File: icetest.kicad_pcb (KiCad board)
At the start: 2 copper layers, 66.7 x 57.2 mm, 50 parts

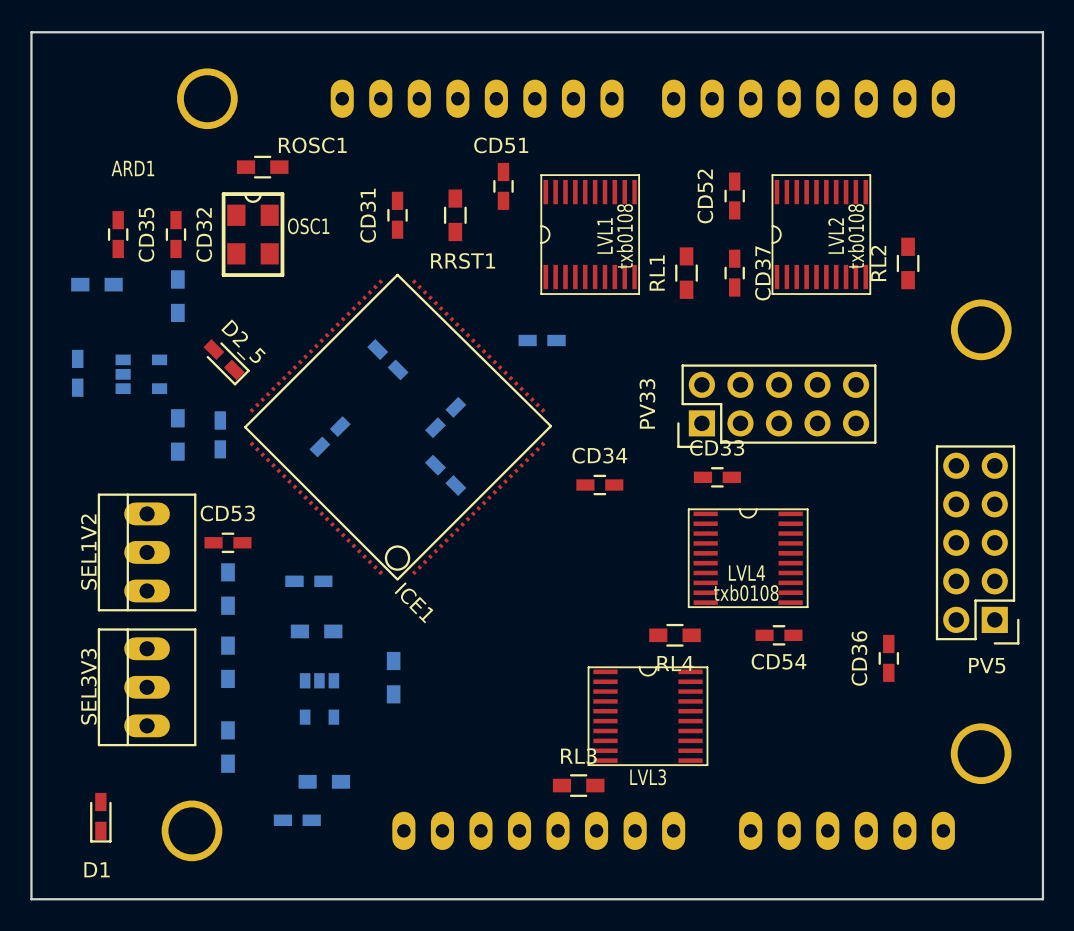
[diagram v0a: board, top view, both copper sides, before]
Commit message: add SPI test points and verify footprints
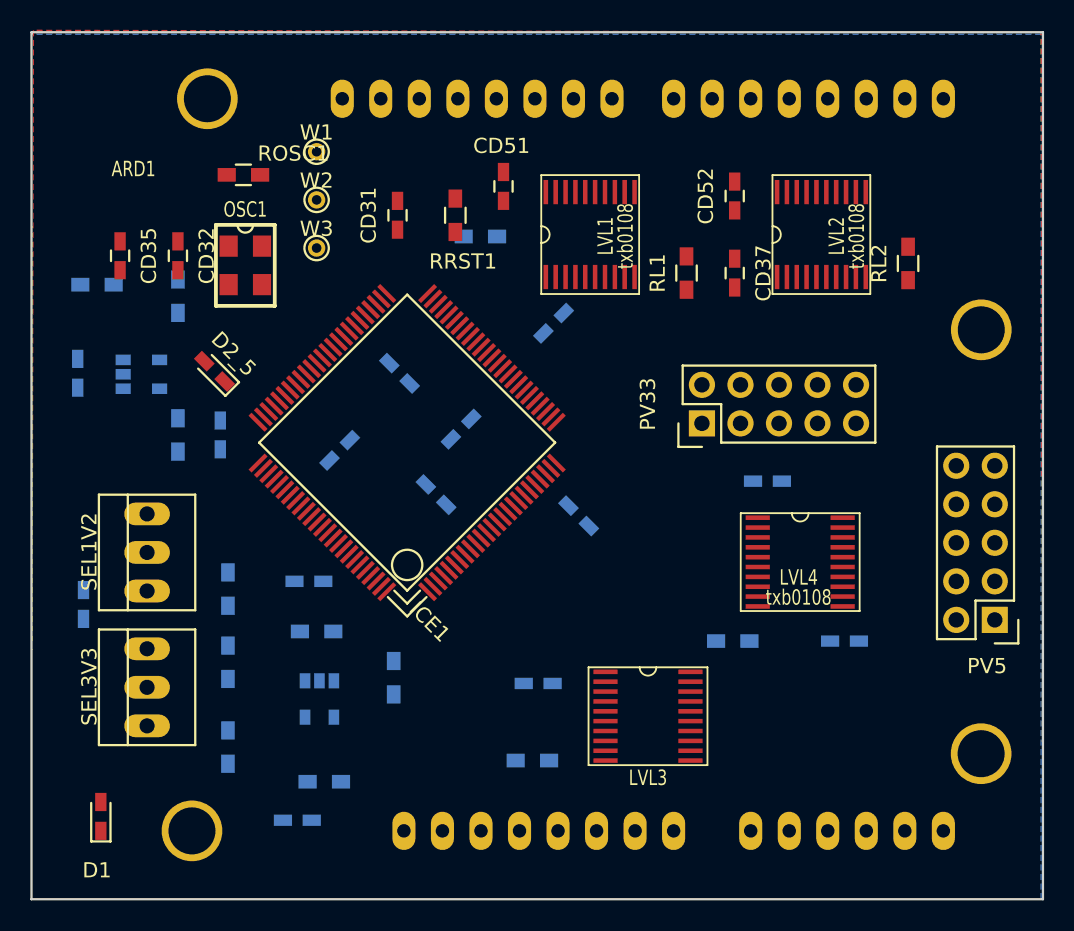
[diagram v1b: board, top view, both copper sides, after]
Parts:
- added RSS1: 10k, Resistors_SMD:R_0603_HandSoldering, B.Cu at (152.8, 106.8)
- added W1: TEST_1P, Connect:PINTST, F.Cu at (142.0, 101.2)
- added W2: TEST_1P, Connect:PINTST, F.Cu at (142.0, 104.4)
- added W3: TEST_1P, Connect:PINTST, F.Cu at (142.0, 107.6)
- CD33, CD34, CD36, CD53, CD54, RL3, RL4: moved to B.Cu
- moved CD36 23.2 mm to (156.6, 136.3), turned to 180 degrees
- moved CD53 10.4 mm to (126.6, 131.1), turned to 270 degrees
- moved CD54 4.33 mm to (176.8, 133.5)
- moved RL4 3.83 mm to (169.4, 133.5)
- moved RL3 3.47 mm to (156.2, 141.4), turned to 180 degrees
- moved LVL4 3.44 mm to (173.9, 128.3)
- moved CD33 3.31 mm to (171.7, 122.9), turned to 180 degrees
- moved CD34 2.47 mm to (159.3, 125.2), turned to 315 degrees
- moved OSC1 2.09 mm to (137.3, 108.7)
- moved CD13 1.42 mm to (149.9, 123.8)
- moved CD32 1.40 mm to (132.8, 108.1)
- moved CD35 1.40 mm to (129.0, 108.1)
- moved CD38 1.37 mm to (157.6, 112.5), turned to 45 degrees
- moved ROSC1 1.37 mm to (137.2, 102.7)
- moved CD14 1.27 mm to (151.5, 119.5)
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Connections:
- CR32 pad 1: GND -> /r3V3
- CR32 pad 2: /r3V3 -> GND
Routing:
- added copper zone on B.Cu, net GND
- added copper zone on F.Cu, net GND
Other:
- net class Ground added: clearance 0.152, trace_width 0.2, via_dia 0.6, via_drill 0.4

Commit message: route it
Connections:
- ARD1 pad 33: (no net) -> GND
- ARD1 pad 34: (no net) -> GND
- ARD1 pad 35: (no net) -> GND
- ARD1 pad 36: (no net) -> GND
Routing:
- net +3V3: track 0.00 -> 213.1 mm, vias 0 -> 4
- net +5V: track 0.00 -> 180.2 mm
- net GND: track 0.00 -> 91.6 mm, vias 0 -> 25
- net VCC: track 0.00 -> 63.9 mm, vias 0 -> 3
- net /FPGA/D5+: track 0.00 -> 52.1 mm, vias 0 -> 1
- net /r3V3: track 0.00 -> 37.1 mm, vias 0 -> 1
- net Net-(ICE1-Pad100): track 0.00 -> 32.7 mm, vias 0 -> 2
- net /FPGA/D5-: track 0.00 -> 32.5 mm, vias 0 -> 1
- net /Arduino Shield/SCK: track 0.00 -> 29.6 mm
- net /Arduino Shield/a3V3: track 0.00 -> 28.9 mm
- net /Arduino Shield/LOG_L3E: track 0.00 -> 28.6 mm, vias 0 -> 2
- net /Arduino Shield/LOG_L2E: track 0.00 -> 27.8 mm
- net /Arduino Shield/ANA0: track 0.00 -> 26.5 mm
- net /Arduino Shield/ANA1: track 0.00 -> 25.4 mm
- net /Arduino Shield/DIG4: track 0.00 -> 25.3 mm, vias 0 -> 2
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
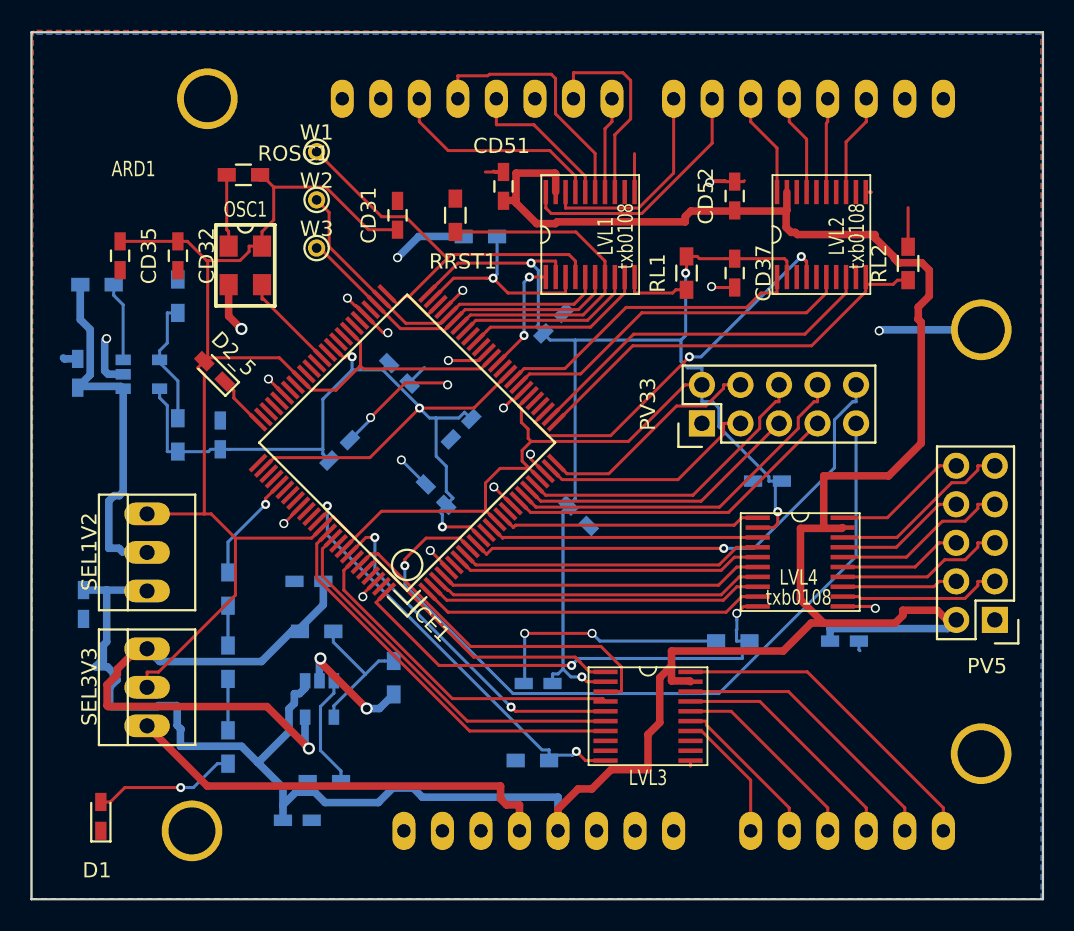
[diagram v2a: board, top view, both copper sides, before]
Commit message: fix ard symbol and route
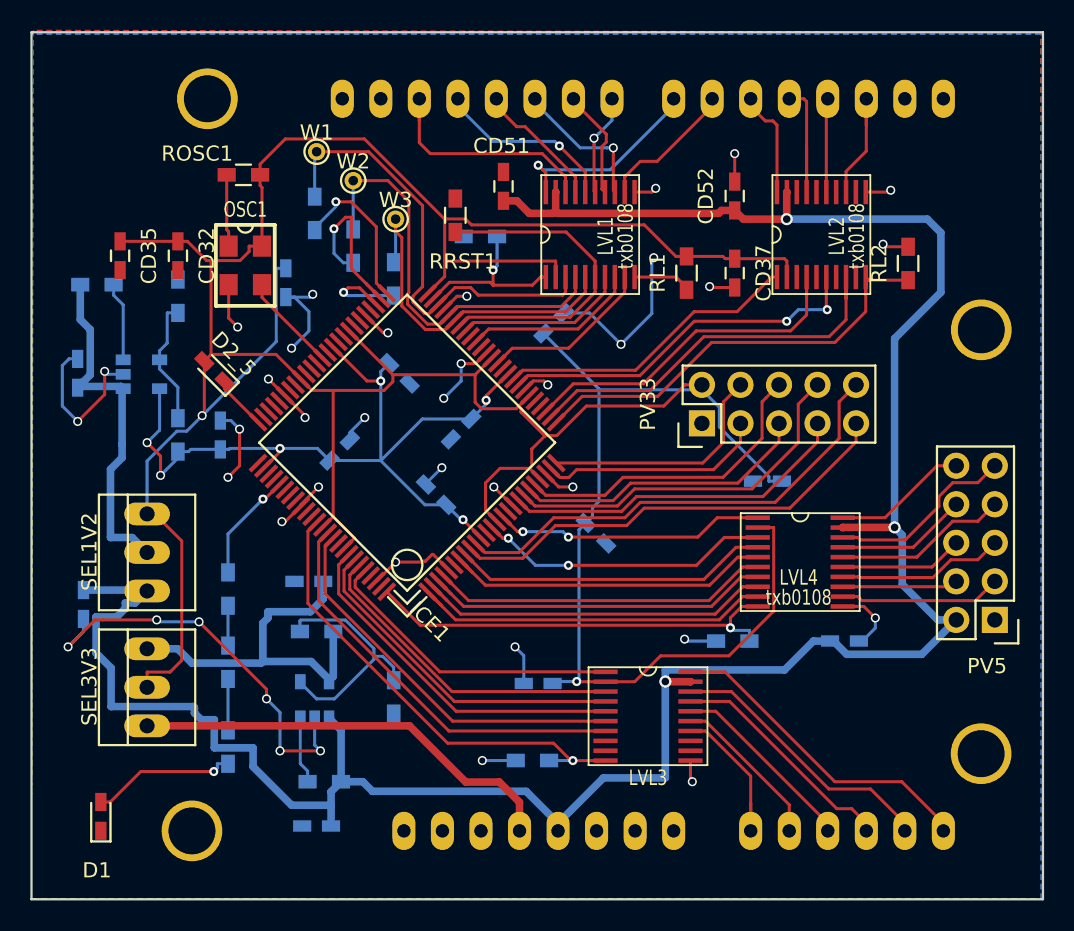
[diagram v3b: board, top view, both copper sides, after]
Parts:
- added J1: R, Resistors_SMD:R_0603_HandSoldering, B.Cu at (141.9, 105.3)
- added J2: R, Resistors_SMD:R_0603_HandSoldering, B.Cu at (144.4, 107.4)
- added J3: R, Resistors_SMD:R_0603_HandSoldering, B.Cu at (147.1, 109.6)
- CD31: moved to B.Cu
- moved CD31 8.60 mm to (140.0, 109.9), turned to 270 degrees
- moved W3 5.54 mm to (147.2, 105.7)
- moved REG3V3 2.85 mm to (142.8, 138.5), turned to 0 degrees
- moved W2 2.73 mm to (144.4, 103.1)
- moved CD34 1.62 mm to (160.4, 126.4)
- moved CR31 1.33 mm to (142.0, 145.7), turned to 180 degrees
- moved R333 1.27 mm to (147.1, 137.2)
- turned R331 to 180 degrees
- turned R332 to 180 degrees
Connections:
- ARD1 pad 25: (no net) -> /Arduino Shield/aD10
- ICE1 pad 51: /Arduino Shield/SCK -> Net-(ICE1-Pad51)
- ICE1 pad 52: /Arduino Shield/MOSI -> Net-(ICE1-Pad52)
- ICE1 pad 53: /Arduino Shield/MISO -> Net-(ICE1-Pad53)
- LVL1 pad 1: /Arduino Shield/DIG6 -> /Arduino Shield/ICE_SS
- LVL1 pad 12: /Arduino Shield/aD10 -> /Arduino Shield/aD6
- LVL1 pad 13: /Arduino Shield/aD9 -> /Arduino Shield/aD10
- LVL1 pad 14: /Arduino Shield/aD8 -> /Arduino Shield/aD9
- LVL1 pad 15: /Arduino Shield/aMISO -> /Arduino Shield/aD8
- LVL1 pad 16: /Arduino Shield/aMOSI -> /Arduino Shield/aMISO
- LVL1 pad 17: /Arduino Shield/aSCK -> /Arduino Shield/aMOSI
- LVL1 pad 18: /Arduino Shield/aD7 -> /Arduino Shield/aSCK
- LVL1 pad 20: /Arduino Shield/aD6 -> /Arduino Shield/aD7
- LVL1 pad 3: /Arduino Shield/ICE_SS -> /Arduino Shield/SCK
- LVL1 pad 4: /Arduino Shield/SCK -> /Arduino Shield/MOSI
- LVL1 pad 5: /Arduino Shield/MOSI -> /Arduino Shield/MISO
- LVL1 pad 6: /Arduino Shield/MISO -> /Arduino Shield/ICE_RST
- LVL1 pad 7: /Arduino Shield/ICE_RST -> /Arduino Shield/ICE_CDONE
- LVL1 pad 8: /Arduino Shield/ICE_CDONE -> /Arduino Shield/DIG10
- LVL1 pad 9: /Arduino Shield/DIG10 -> /Arduino Shield/DIG6
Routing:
- net +3V3: track 213.1 -> 246.8 mm, vias 4 -> 2
- net GND: track 91.6 -> 116.3 mm, vias 25 -> 39
- net /FPGA/D5+: track 52.1 -> 30.5 mm, vias 1 -> 0
- net +5V: track 180.2 -> 161.9 mm, vias 0 -> 3
- net Net-(ICE1-Pad52): track 0.00 -> 12.2 mm, vias 0 -> 1
- net /r3V3: track 37.1 -> 25.0 mm, vias 1 -> 0
- net Net-(ICE1-Pad51): track 0.00 -> 11.0 mm, vias 0 -> 1
- net /Arduino Shield/aD10: track 0.00 -> 9.86 mm, vias 0 -> 1
- net VCC: track 63.9 -> 55.3 mm, vias 3 -> 6
- net /Arduino Shield/aD6: track 17.0 -> 9.44 mm
- net Net-(ICE1-Pad53): track 0.00 -> 6.87 mm, vias 0 -> 1
- net Net-(R332-Pad2): track 9.61 -> 16.0 mm
- net /Arduino Shield/aD9: track 13.5 -> 7.55 mm
- net /Arduino Shield/aMISO: track 16.7 -> 12.3 mm, vias 0 -> 1
- net Net-(ICE1-Pad100): track 32.7 -> 28.4 mm, vias 2 -> 1
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
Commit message: remove dup pins from symbols
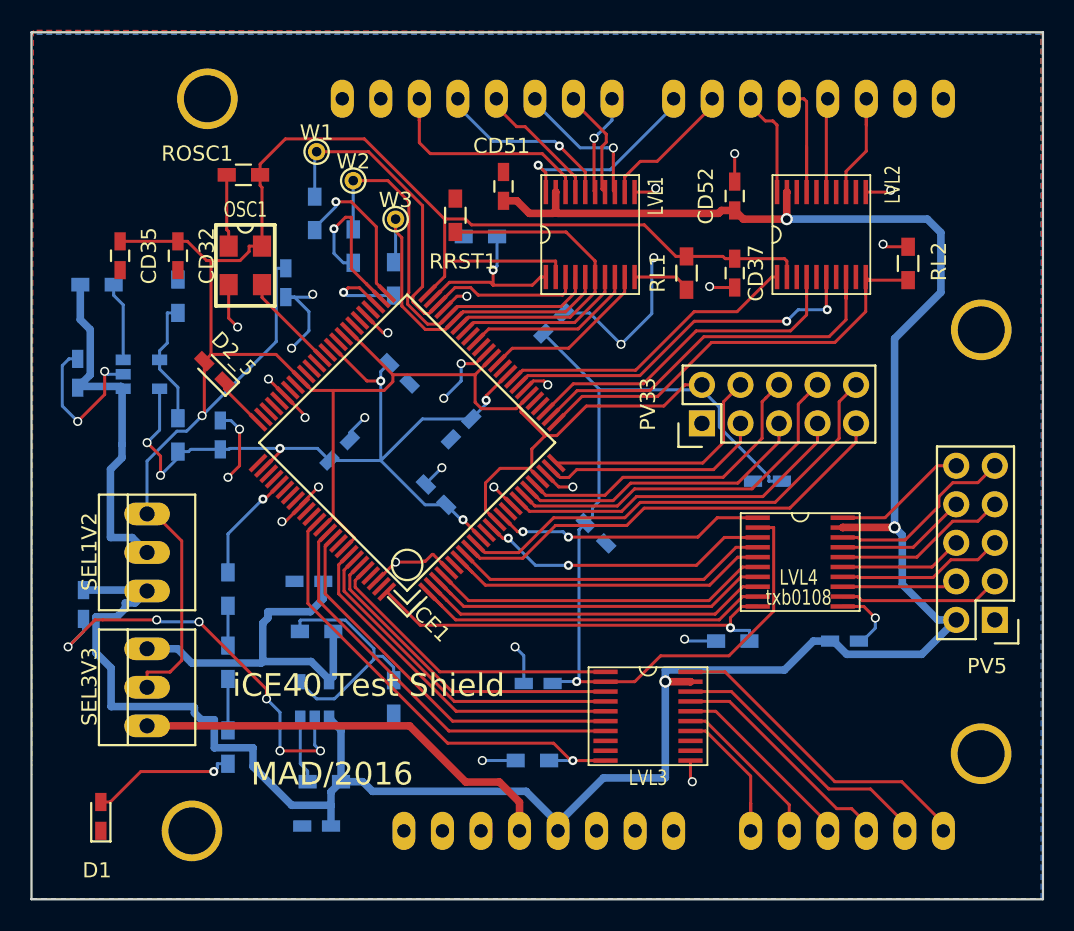
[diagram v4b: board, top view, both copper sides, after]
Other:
- board text added: "MAD/2016"
- board text removed: "MaD/2016"
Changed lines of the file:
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@@
     (area 123.114999 50.227999 191.798334 150.570001)
     (thickness 1.6)
-    (drawings 7)
+    (drawings 9)
     (tracks 1092)
     (zones 0)
@@
   (module local:PSO_20 (layer F.Cu)
     (at 160.02 106.68 90)
-    (fp_text reference LVL1 (at -0.1016 1.016 90) (layer F.SilkS)
+    (fp_text reference LVL1 (at 2.54 4.318 90) (layer F.SilkS)
       (effects (font (size 1.016 0.762) (thickness 0.127)))
     )
-    (fp_text value txb0108 (at -0.1016 2.3368 90) (layer F.SilkS)
+    (fp_text value txb0108 (at -0.1016 2.3368 90) (layer F.SilkS) hide
       (effects (font (size 1.016 0.762) (thickness 0.127)))
     )
@@
   (module local:PSO_20 (layer F.Cu)
     (at 175.26 106.68 90)
-    (fp_text reference LVL2 (at -0.1016 1.016 90) (layer F.SilkS)
+    (fp_text reference LVL2 (at 3.302 4.699 90) (layer F.SilkS)
       (effects (font (size 1.016 0.762) (thickness 0.127)))
     )
-    (fp_text value txb0108 (at -0.1016 2.3368 90) (layer F.SilkS)
+    (fp_text value txb0108 (at -0.1016 2.3368 90) (layer F.SilkS) hide
       (effects (font (size 1.016 0.762) (thickness 0.127)))
     )
@@
     (tags "capacitor 0603")
     (attr smd)
-    (fp_text reference CR11 (at 0 1.9 90) (layer B.SilkS)
+    (fp_text reference CR11 (at 0 1.524 90) (layer B.SilkS)
       (effects (font (size 1 1) (thickness 0.15)) (justify mirror))
     )
@@
     (tags "capacitor 0603")
     (attr smd)
-    (fp_text reference CD37 (at 0 -1.9 270) (layer F.SilkS)
+    (fp_text reference CD37 (at 0 -1.397 270) (layer F.SilkS)
       (effects (font (size 1 1) (thickness 0.15)))
     )
@@
     (tags "resistor 0603")
     (attr smd)
-    (fp_text reference R333 (at 0 1.9 270) (layer B.SilkS)
+    (fp_text reference R333 (at 0.127 -1.778 270) (layer B.SilkS)
       (effects (font (size 1 1) (thickness 0.15)) (justify mirror))
     )
@@
     (tags "resistor 0603")
     (attr smd)
-    (fp_text reference RL2 (at 0 -1.9 90) (layer F.SilkS)
+    (fp_text reference RL2 (at 0.127 2.032 90) (layer F.SilkS)
       (effects (font (size 1 1) (thickness 0.15)))
     )
@@
   (module local:SOT23-5 (layer B.Cu)
     (at 129.286 116.84 270)
-    (fp_text reference REG1V2 (at 2.159 -0.508 270) (layer B.SilkS)
+    (fp_text reference REG1V2 (at 2.921 -0.889 270) (layer B.SilkS)
       (effects (font (size 1.016 0.762) (thickness 0.127)) (justify mirror))
     )
-    (fp_text value regulator5 (at 2.286 -2.413 270) (layer B.SilkS)
+    (fp_text value regulator5 (at 3.937 2.286 270) (layer B.SilkS) hide
       (effects (font (size 1.016 0.762) (thickness 0.127)) (justify mirror))
     )
@@
     )
   )
+  (gr_text "iCE40 Test Shield" (at 145.415 136.398) (layer F.SilkS)
+    (effects (font (size 1.5 1.5) (thickness 0.3)))
+  )
+  (gr_text MAD/2016 (at 143.002 142.24) (layer F.SilkS)
+    (effects (font (size 1.5 1.5) (thickness 0.3)))
+  )
   (gr_circle (center 173.942 62.458) (end 186.072 62.458) (layer Dwgs.User) (width 0.2))
-  (gr_text MaD/2016 (at 168.148 105.41) (layer B.SilkS)
+  (gr_text MAD/2016 (at 170.815 108.839) (layer B.SilkS)
     (effects (font (size 1.5 1.5) (thickness 0.3)) (justify mirror))
   )
-  (gr_text "iCE40 Test Shield" (at 168.402 109.982) (layer B.SilkS)
+  (gr_text "iCE40 Test Shield" (at 172.212 113.157) (layer B.SilkS)
     (effects (font (size 1.5 1.5) (thickness 0.3)) (justify mirror))
   )

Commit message: update layout
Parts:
- removed R332, R333: R, Resistors_SMD:R_0603_HandSoldering
- added RCLK1: 10k, Resistors_SMD:R_0603_HandSoldering, B.Cu at (137.5, 103.1)
- added RDON1: 10k, Resistors_SMD:R_0603_HandSoldering, B.Cu at (152.5, 112.3)
- ROSC1: value R -> 10k
- moved R122 2.33 mm to (130.7, 120.8), turned to 0 degrees
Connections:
- R122 pad 1: VCC -> /iVcc
- RRST1 pad 2: GND -> +3V3
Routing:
- net GND: track 116.3 -> 168.5 mm, vias 39 -> 48
- net Net-(REG3V3-Pad4): track 16.0 -> 0.00 mm
- net +3V3: track 246.8 -> 261.0 mm
- net +5V: track 161.9 -> 153.9 mm
- net VCC: track 55.3 -> 50.0 mm, vias 6 -> 4
- net /Arduino Shield/ICE_CDONE: track 11.8 -> 15.6 mm, vias 0 -> 1
- net /r3V3: track 25.0 -> 21.2 mm
- net /Arduino Shield/SCK: track 30.5 -> 34.1 mm
- net /FPGA/xD1-: track 7.63 -> 10.7 mm
- net Net-(R122-Pad2): track 8.35 -> 11.3 mm
- net /FPGA/xD2-: track 8.15 -> 11.0 mm
- net /FPGA/xD3-: track 8.66 -> 11.5 mm
- net /FPGA/D10+: track 20.0 -> 21.3 mm
- net /FPGA/D5+: track 30.5 -> 31.8 mm
- net /FPGA/D8+: track 23.5 -> 24.8 mm
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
